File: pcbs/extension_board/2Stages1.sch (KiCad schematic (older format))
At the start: 9 parts, among them Q1 MBT3904DW1, U1 LM324QT

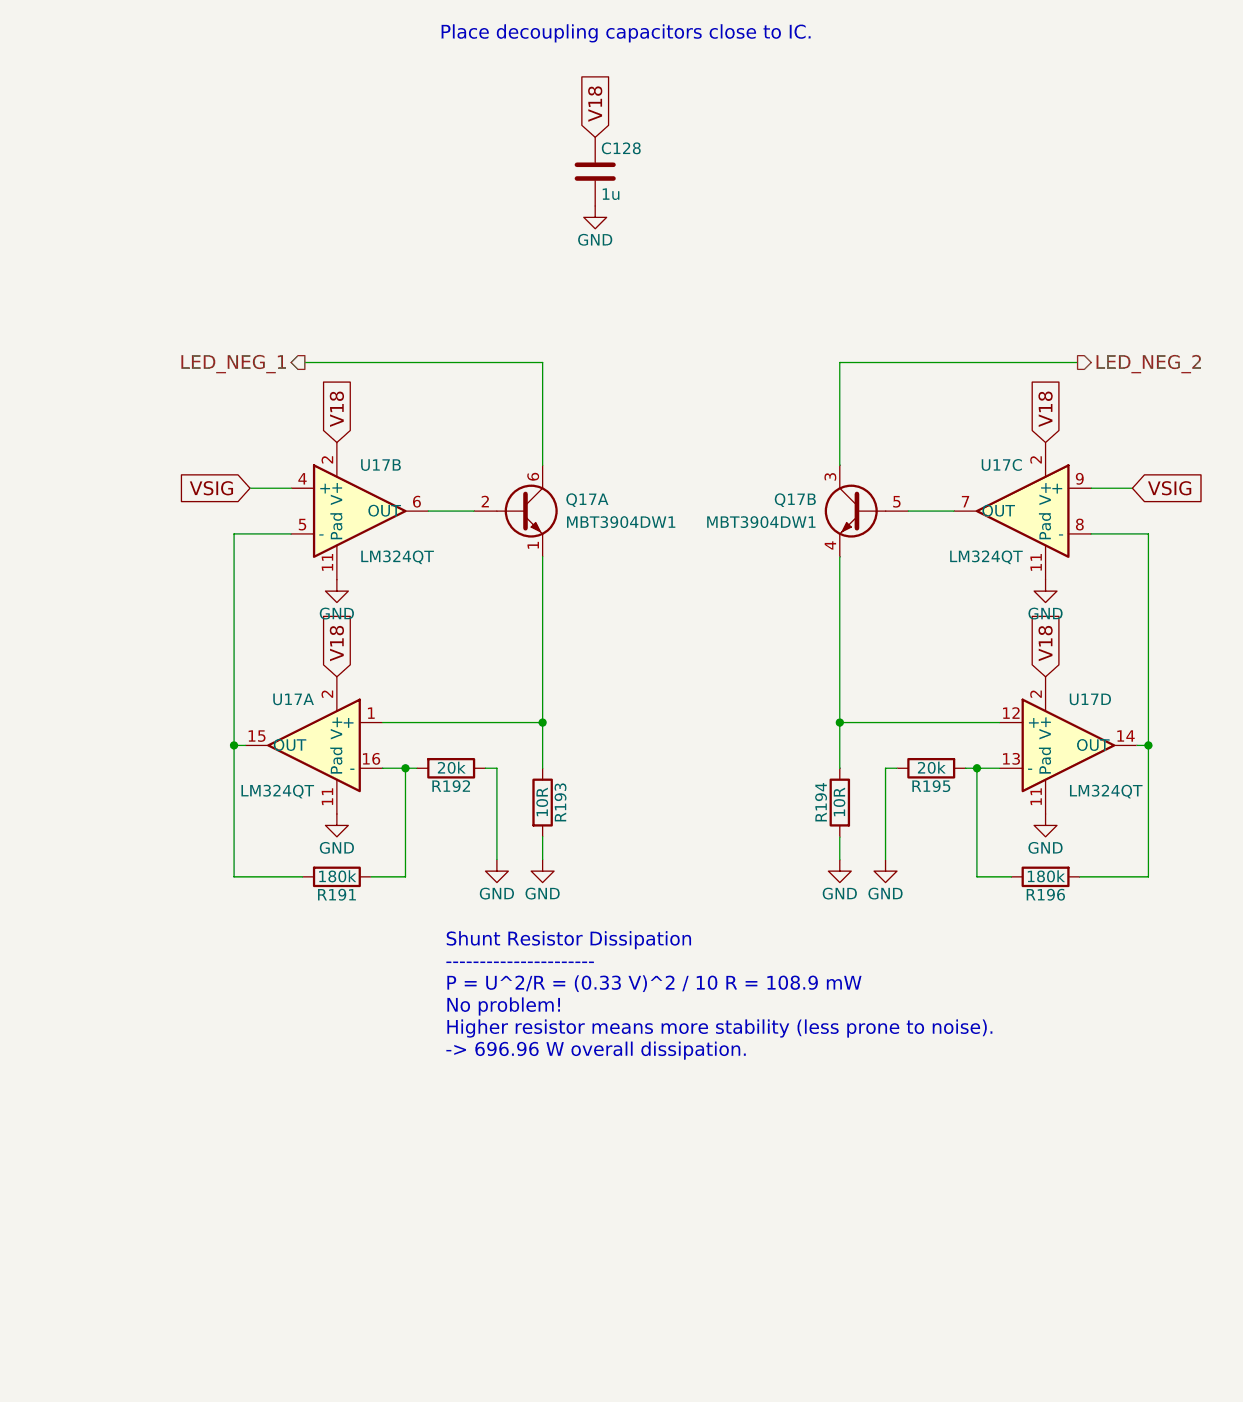
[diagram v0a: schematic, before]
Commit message: Changed transistor array of driver for SOT-23 discrete transistor (more dissipation allowed).
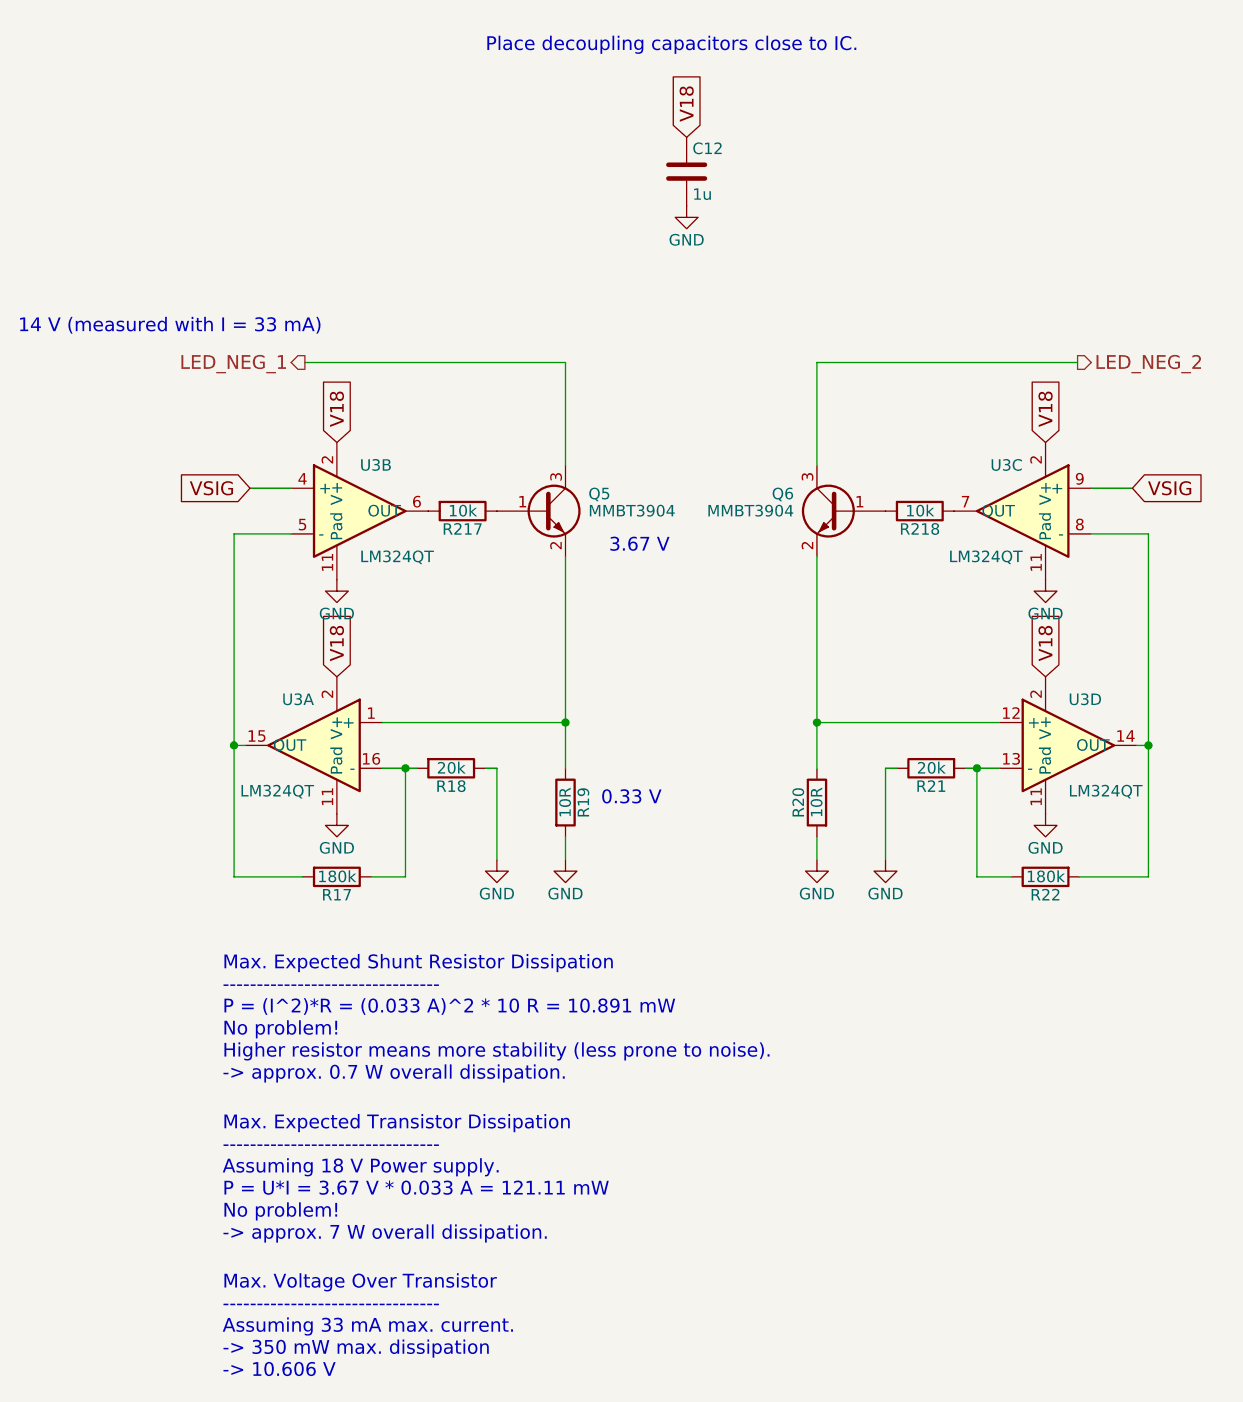
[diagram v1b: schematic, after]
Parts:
- removed Q1: MBT3904DW1, TO_SOT_Packages_SMD:SOT-363_SC-70-6, symbol MBT3904DW1
- added Q1, Q2: MMBT3904, TO_SOT_Packages_SMD:SOT-23, symbol MMBT3904
- added R213, R214: 10k, Resistors_SMD:R_0603, symbol R
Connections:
- net LED_NEG_1: now also Q1.3 (C)
- net LED_NEG_2: now also Q2.3 (C)
- net at R8.1, U1.12 (+): now also Q2.2 (E)
- net at U1.7 (OUT): now also R214.1
- net at R7.1, U1.1 (+): now also Q1.2 (E)
- net at U1.6 (OUT): now also R213.2
- new net: Q1.1 (B), R213.1
- new net: Q2.1 (B), R214.2
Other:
- note added: "0.33 V"
- note added: "14 V (measured with I = 33 mA)"
- note added: "3.67 V"
- note added: "Max. Expected Shunt Resistor Dissipation\n--------------------------------\nP = (I^2)*R = (0.033 A)^2 * 10 R = 10.891 mW\nNo problem!\nHigher resistor means more stability (less prone to noise).\n-> approx. 0.7 W overall dissipation."
- note added: "Max. Expected Transistor Dissipation\n--------------------------------\nAssuming 18 V Power supply.\nP = U*I = 3.67 V * 0.033 A = 121.11 mW\nNo problem!\n-> approx. 7 W overall dissipation."
- note added: "Max. Voltage Over Transistor\n--------------------------------\nAssuming 33 mA max. current.\n-> 350 mW max. dissipation \n-> 10.606 V"
- note removed: "Shunt Resistor Dissipation\n----------------------\nP = U^2/R = (0.33 V)^2 / 10 R = 108.9 mW\nNo problem!\nHigher resistor means more stability (less prone to noise).\n-> 696.96 W overall dissipation."
- moved on the sheet: C12, R19, R20

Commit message: Produced Gerber files for both boards. Ready for production.
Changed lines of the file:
@@
 $Descr A4 11693 8268
 encoding utf-8
-Sheet 3 37
+Sheet 26 37
 Title "UV LED Driver Two Stages"
 Date "2017-11-13"
@@
 AR Path="/5A0916C5/5A09BEE8/5946B2F2" Ref="C124"  Part="1"
 AR Path="/5A0916C5/5A09BEEC/5946B2F2" Ref="C128"  Part="1"
-F 0 "C12" H 5905 2065 50  0000 L CNN
+F 0 "C96" H 5905 2065 50  0000 L CNN
 F 1 "1u" H 5905 1865 50  0000 L CNN
 F 2 "Resistors_SMD:R_0603" H 5918 1815 50  0001 C CNN
@@
 AR Path="/5A0916C5/5A09BEE8/5A08DFEB" Ref="R188"  Part="1"
 AR Path="/5A0916C5/5A09BEEC/5A08DFEB" Ref="R194"  Part="1"
-F 0 "R20" V 6530 4725 50  0000 C CNN
+F 0 "R146" V 6530 4725 50  0000 C CNN
 F 1 "10R" V 6450 4725 50  0000 C CNN
 F 2 "Resistors_SMD:R_0603" V 6380 4725 50  0001 C CNN
@@
 AR Path="/5A0916C5/5A09BEE8/5A08DFF3" Ref="R190"  Part="1"
 AR Path="/5A0916C5/5A09BEEC/5A08DFF3" Ref="R196"  Part="1"
-F 0 "R22" V 7530 5050 50  0000 C CNN
+F 0 "R148" V 7530 5050 50  0000 C CNN
 F 1 "180k" V 7450 5050 50  0000 C CNN
 F 2 "Resistors_SMD:R_0603" V 7380 5050 50  0001 C CNN
@@
 AR Path="/5A0916C5/5A09BEE8/5A08DFFA" Ref="R189"  Part="1"
 AR Path="/5A0916C5/5A09BEEC/5A08DFFA" Ref="R195"  Part="1"
-F 0 "R21" V 7030 4575 50  0000 C CNN
+F 0 "R147" V 7030 4575 50  0000 C CNN
 F 1 "20k" V 6950 4575 50  0000 C CNN
 F 2 "Resistors_SMD:R_0603" V 6880 4575 50  0001 C CNN
@@
 AR Path="/5A0916C5/5A09BEE8/5A08E007" Ref="U18"  Part="3"
 AR Path="/5A0916C5/5A09BEEC/5A08E007" Ref="U17"  Part="3"
-F 0 "U3" H 7350 3650 50  0000 L CNN
+F 0 "U25" H 7350 3650 50  0000 L CNN
 F 1 "LM324QT" H 7350 3250 50  0000 L CNN
 F 2 "QFN:QFN-16-1EP_3x3mm_Pitch0.5mm" H 7300 3550 50  0001 C CNN
@@
 AR Path="/5A0916C5/5A09BEE8/5A08E00E" Ref="U18"  Part="4"
 AR Path="/5A0916C5/5A09BEEC/5A08E00E" Ref="U17"  Part="4"
-F 0 "U3" H 7550 4675 50  0000 L CNN
+F 0 "U25" H 7550 4675 50  0000 L CNN
 F 1 "LM324QT" H 7550 4275 50  0000 L CNN
 F 2 "QFN:QFN-16-1EP_3x3mm_Pitch0.5mm" H 7500 4575 50  0001 C CNN
@@
 AR Path="/5A0916C5/5A09BEE8/5A08E015" Ref="#PWR0274"  Part="1"
 AR Path="/5A0916C5/5A09BEEC/5A08E015" Ref="#PWR0283"  Part="1"
-F 0 "#PWR022" H 7450 3500 50  0001 C CNN
+F 0 "#PWR0211" H 7450 3500 50  0001 C CNN
 F 1 "GND" H 7450 3600 50  0000 C CNN
 F 2 "" H 7450 3750 50  0001 C CNN
@@
 AR Path="/5A0916C5/5A09BEE8/5A08E01B" Ref="#PWR0275"  Part="1"
 AR Path="/5A0916C5/5A09BEEC/5A08E01B" Ref="#PWR0284"  Part="1"
-F 0 "#PWR023" H 7450 4525 50  0001 C CNN
+F 0 "#PWR0212" H 7450 4525 50  0001 C CNN
 F 1 "GND" H 7450 4625 50  0000 C CNN
 F 2 "" H 7450 4775 50  0001 C CNN
@@
 AR Path="/5A0916C5/5A09BEE8/5A08E02C" Ref="#PWR0276"  Part="1"
 AR Path="/5A0916C5/5A09BEEC/5A08E02C" Ref="#PWR0285"  Part="1"
-F 0 "#PWR024" H 6750 4725 50  0001 C CNN
+F 0 "#PWR0213" H 6750 4725 50  0001 C CNN
 F 1 "GND" H 6750 4825 50  0000 C CNN
 F 2 "" H 6750 4975 50  0001 C CNN
@@
 AR Path="/5A0916C5/5A09BEE8/5A08E038" Ref="#PWR0277"  Part="1"
 AR Path="/5A0916C5/5A09BEEC/5A08E038" Ref="#PWR0286"  Part="1"
-F 0 "#PWR025" H 6450 4725 50  0001 C CNN
+F 0 "#PWR0214" H 6450 4725 50  0001 C CNN
 F 1 "GND" H 6450 4825 50  0000 C CNN
 F 2 "" H 6450 4975 50  0001 C CNN
@@
 AR Path="/5A0916C5/5A09BEE8/5A15979F" Ref="R187"  Part="1"
 AR Path="/5A0916C5/5A09BEEC/5A15979F" Ref="R193"  Part="1"
-F 0 "R19" V 5430 4725 50  0000 C CNN
+F 0 "R145" V 5430 4725 50  0000 C CNN
 F 1 "10R" V 5350 4725 50  0000 C CNN
 F 2 "Resistors_SMD:R_0603" V 5280 4725 50  0001 C CNN
@@
 AR Path="/5A0916C5/5A09BEE8/5A1597A7" Ref="R185"  Part="1"
 AR Path="/5A0916C5/5A09BEEC/5A1597A7" Ref="R191"  Part="1"
-F 0 "R17" V 4430 5050 50  0000 C CNN
+F 0 "R143" V 4430 5050 50  0000 C CNN
 F 1 "180k" V 4350 5050 50  0000 C CNN
 F 2 "Resistors_SMD:R_0603" V 4280 5050 50  0001 C CNN
@@
 AR Path="/5A0916C5/5A09BEE8/5A1597AE" Ref="R186"  Part="1"
 AR Path="/5A0916C5/5A09BEEC/5A1597AE" Ref="R192"  Part="1"
-F 0 "R18" V 4930 4575 50  0000 C CNN
+F 0 "R144" V 4930 4575 50  0000 C CNN
 F 1 "20k" V 4850 4575 50  0000 C CNN
 F 2 "Resistors_SMD:R_0603" V 4780 4575 50  0001 C CNN
@@
 AR Path="/5A0916C5/5A09BEE8/5A1597B5" Ref="U18"  Part="2"
 AR Path="/5A0916C5/5A09BEEC/5A1597B5" Ref="U17"  Part="2"
-F 0 "U3" H 4450 3650 50  0000 L CNN
+F 0 "U25" H 4450 3650 50  0000 L CNN
 F 1 "LM324QT" H 4450 3250 50  0000 L CNN
 F 2 "QFN:QFN-16-1EP_3x3mm_Pitch0.5mm" H 4400 3550 50  0001 C CNN
@@
 AR Path="/5A0916C5/5A09BEE8/5A1597BC" Ref="U18"  Part="1"
 AR Path="/5A0916C5/5A09BEEC/5A1597BC" Ref="U17"  Part="1"
-F 0 "U3" H 4250 4675 50  0000 L CNN
+F 0 "U25" H 4250 4675 50  0000 L CNN
 F 1 "LM324QT" H 4250 4275 50  0000 L CNN
 F 2 "QFN:QFN-16-1EP_3x3mm_Pitch0.5mm" H 4200 4575 50  0001 C CNN
@@
 AR Path="/5A0916C5/5A09BEE8/5A1597C3" Ref="#PWR0278"  Part="1"
 AR Path="/5A0916C5/5A09BEEC/5A1597C3" Ref="#PWR0287"  Part="1"
-F 0 "#PWR026" H 4350 3500 50  0001 C CNN
+F 0 "#PWR0215" H 4350 3500 50  0001 C CNN
 F 1 "GND" H 4350 3600 50  0000 C CNN
 F 2 "" H 4350 3750 50  0001 C CNN
@@
 AR Path="/5A0916C5/5A09BEE8/5A1597C9" Ref="#PWR0279"  Part="1"
 AR Path="/5A0916C5/5A09BEEC/5A1597C9" Ref="#PWR0288"  Part="1"
-F 0 "#PWR027" H 4350 4525 50  0001 C CNN
+F 0 "#PWR0216" H 4350 4525 50  0001 C CNN
 F 1 "GND" H 4350 4625 50  0000 C CNN
 F 2 "" H 4350 4775 50  0001 C CNN
@@
 AR Path="/5A0916C5/5A09BEE8/5A1597DA" Ref="#PWR0280"  Part="1"
 AR Path="/5A0916C5/5A09BEEC/5A1597DA" Ref="#PWR0289"  Part="1"
-F 0 "#PWR028" H 5050 4725 50  0001 C CNN
+F 0 "#PWR0217" H 5050 4725 50  0001 C CNN
 F 1 "GND" H 5050 4825 50  0000 C CNN
 F 2 "" H 5050 4975 50  0001 C CNN
@@
 AR Path="/5A0916C5/5A09BEE8/5A1597E6" Ref="#PWR0281"  Part="1"
 AR Path="/5A0916C5/5A09BEEC/5A1597E6" Ref="#PWR0290"  Part="1"
-F 0 "#PWR029" H 5350 4725 50  0001 C CNN
+F 0 "#PWR0218" H 5350 4725 50  0001 C CNN
 F 1 "GND" H 5350 4825 50  0000 C CNN
 F 2 "" H 5350 4975 50  0001 C CNN
@@
 AR Path="/5A0916C5/5A09BEE8/5946B480" Ref="#PWR0282"  Part="1"
 AR Path="/5A0916C5/5A09BEEC/5946B480" Ref="#PWR0291"  Part="1"
-F 0 "#PWR030" H 5880 1865 50  0001 C CNN
+F 0 "#PWR0219" H 5880 1865 50  0001 C CNN
 F 1 "GND" H 5880 1965 50  0000 C CNN
 F 2 "" H 5880 2115 50  0000 C CNN
@@
 AR Path="/5A0916C5/5A09BEE8/5A1FEC0D" Ref="Q35"  Part="1"
 AR Path="/5A0916C5/5A09BEEC/5A1FEC0D" Ref="Q33"  Part="1"
-F 0 "Q5" H 5450 3525 50  0000 L CNN
+F 0 "Q49" H 5450 3525 50  0000 L CNN
 F 1 "MMBT3904" H 5450 3450 50  0000 L CNN
 F 2 "TO_SOT_Packages_SMD:SOT-23" H 5450 3375 50  0001 L CIN
@@
 AR Path="/5A0916C5/5A09BEE8/5A1FEFA7" Ref="Q36"  Part="1"
 AR Path="/5A0916C5/5A09BEEC/5A1FEFA7" Ref="Q34"  Part="1"
-F 0 "Q6" H 6750 3525 50  0000 L CNN
+F 0 "Q50" H 6750 3525 50  0000 L CNN
 F 1 "MMBT3904" H 6750 3450 50  0000 L CNN
 F 2 "TO_SOT_Packages_SMD:SOT-23" H 6750 3375 50  0001 L CIN
@@
 AR Path="/5A0916C5/5A09BEE8/5A1FF296" Ref="R273"  Part="1"
 AR Path="/5A0916C5/5A09BEEC/5A1FF296" Ref="R275"  Part="1"
-F 0 "R217" V 4980 3450 50  0000 C CNN
+F 0 "R259" V 4980 3450 50  0000 C CNN
 F 1 "10k" V 4900 3450 50  0000 C CNN
 F 2 "Resistors_SMD:R_0603" V 4830 3450 50  0001 C CNN
@@
 AR Path="/5A0916C5/5A09BEE8/5A20118E" Ref="R274"  Part="1"
 AR Path="/5A0916C5/5A09BEEC/5A20118E" Ref="R276"  Part="1"
-F 0 "R218" V 6980 3450 50  0000 C CNN
+F 0 "R260" V 6980 3450 50  0000 C CNN
 F 1 "10k" V 6900 3450 50  0000 C CNN
 F 2 "Resistors_SMD:R_0603" V 6830 3450 50  0001 C CNN
